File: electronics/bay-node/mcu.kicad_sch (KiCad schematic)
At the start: 15 parts, among them SW1 RESET, SW2 BOOT, U3 ESP32-S3-WROOM-1-N8R8

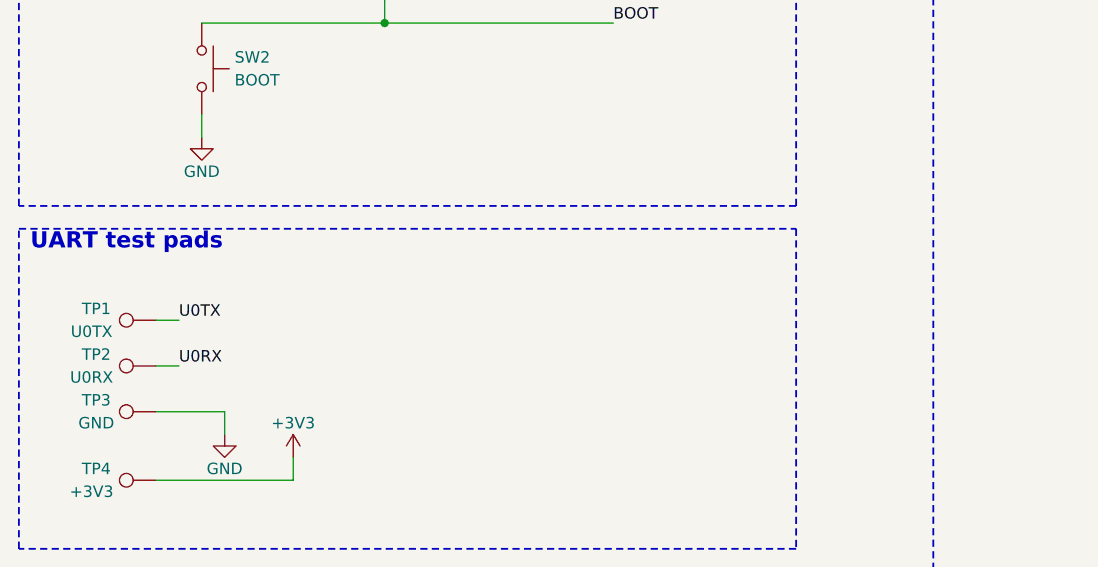
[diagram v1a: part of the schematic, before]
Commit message: Boards: labelled bottom test pads; hub dVdT 100 nF, 50 ms FLT blank
Eve's DFT rule on the four boards this session owns: bare pads on the
bottom, named on B.SilkS, out of the BOM and the CPL (no part, no
assembly fee).  Supply pads 1.5 mm, signal pads 1.0 mm (new catalog
entry "testpad1"), all more than 2 mm from any THT pad or hole
(closest: 4.7 mm, the pod's TP4).  Positions are fixed in design.py,
so they stay put across revisions.

- bay node, 17: TX, RX, 3V3, GND by the module (kept), then EN, IO0,
  FLT (DUT_FLT_N), ALRT (INA_ALERT_N), SDA, SCL and a second GND;
  a supply row along the bottom edge: GND, VIN, 5V, 3V3, DUT 5V,
  CAM 5V
- power hub, 20: TX, RX, 3V3, GND, 5V, VRACK, GND (kept), then EN,
  IO0, the CH224A's PD SDA/SCL, each row's FLT and IMON (A-D) and a
  third GND in the middle
- camera pod, 4: GND, 5V, 3V3 and a second GND at the far end
- DATA port, 2: GND and 5V (VBUS, through a via under its track)

Hub, as the datasheet audit's U1 answer asks (TPS2660 Fig. 55 at
85 C: 8-10 ms at 21 W fails the 47 nF worst start, 33 ms at 14 W
covers 100 nF): C21-C24 dVdT 47 nF -> 100 nF, so a row's soft start
is 16-22 ms and dissipates about 7-9 W typical, 14 W worst, for
19-24 ms; the firmware's HUB_ROW_FLT_BLANK_MS goes 25 -> 50 ms to
cover it (worst case 39 ms).  docs/power.md, the audit row and the
hub notes say so.

Routing fallout: J1's A12/B1 GND now leaves through one drawn 0.5 mm
via so the automatic fan-out can't cut the VRACK pour off A9/B4; the
pod's LDO tab zones are exclusive so tracks no longer split them.

All four rerouted, tidied and checked: ERC 0, DRC 0, unconnected 0,
parity 0.  Gerbers, renders, schematics, viewer GLBs, the JLC
snapshot lines and the rack BOM regenerated.

Co-Authored-By: Claude Opus 5.5 <noreply@anthropic.com>
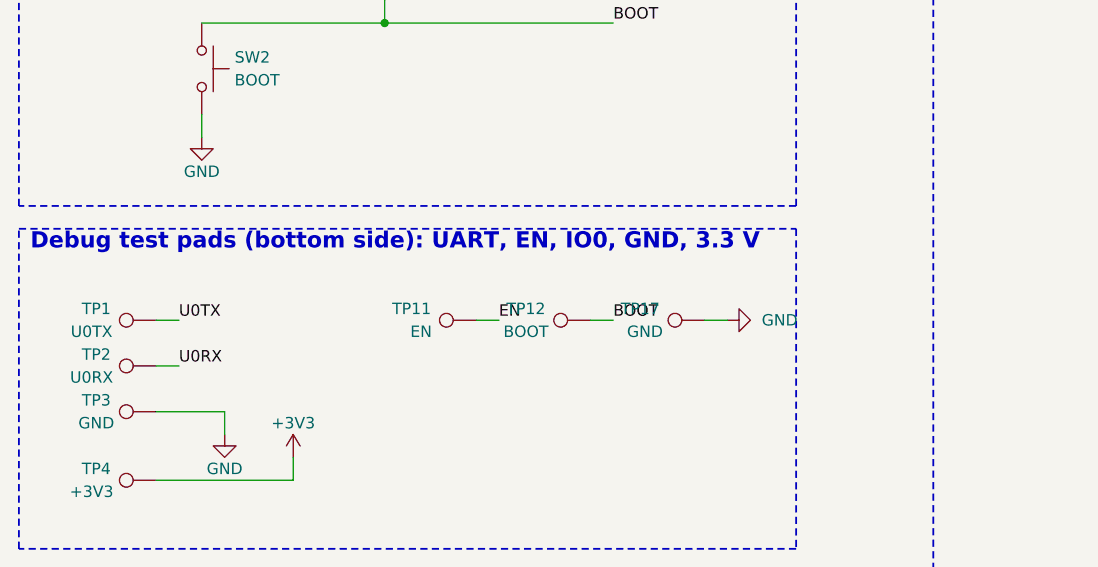
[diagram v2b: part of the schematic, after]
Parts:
- added TP11: EN, TestPoint:TestPoint_Pad_D1.0mm, symbol Connector:TestPoint
- added TP12: BOOT, TestPoint:TestPoint_Pad_D1.0mm, symbol Connector:TestPoint
- added TP17: GND, TestPoint:TestPoint_Pad_D1.5mm, symbol Connector:TestPoint
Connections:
- net BOOT: now also TP12.1
- net EN: now also TP11.1
- net GND: now also TP17.1
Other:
- note added: "Debug test pads (bottom side): UART, EN, IO0, GND, 3.3 V"
- note removed: "UART test pads"
